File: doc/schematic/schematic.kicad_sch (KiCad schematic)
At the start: 22 parts, among them J1 Power, J10 Screw_Terminal_01x02, J11 UART, J12 UART, J13 Power, J14 Conn_01x02_Pin, J15 FX35, J16 FX35, J17 Load, J2 TFT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

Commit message: Schema V0.1
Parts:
- removed J1: Power, symbol Connector:Conn_01x02_Pin
- removed J2: TFT, symbol Connector:Conn_01x06_Pin
- removed J3: TFT_Power, symbol Connector:Conn_01x02_Socket
- removed J4: TFT, symbol Connector:Conn_01x06_Socket
- removed J5: USB_B_Mini, symbol Connector:USB_B_Mini
- added J1: TFT_Power, Connector_Molex:Molex_KK-254_AE-6410-03A_1x03_P2.54mm_Vertical, symbol Connector:Conn_01x03_Pin
- added J18: USB, Connector_Molex:Molex_KK-254_AE-6410-02A_1x02_P2.54mm_Vertical, symbol Connector:Conn_01x02_Pin
- added J19: Switch, Connector_Molex:Molex_KK-254_AE-6410-02A_1x02_P2.54mm_Vertical, symbol Connector:Conn_01x02_Pin
- added J2: Conn_01x03_Socket, Connector_Molex:Molex_KK-254_AE-6410-03A_1x03_P2.54mm_Vertical, symbol Connector:Conn_01x03_Socket
- added J20, J21: Conn_01x02_Socket, symbol Connector:Conn_01x02_Socket
- added J3: TFT, Connector_Molex:Molex_KK-254_AE-6410-05A_1x05_P2.54mm_Vertical, symbol Connector:Conn_01x05_Pin
- added J4: Conn_01x05_Socket, symbol Connector:Conn_01x05_Socket
- added J5: USB_C_PowerOnly, symbol Connector:USB_C_Receptacle_PowerOnly_6P
- added SW1: SW_DIP_x01, symbol Switch:SW_DIP_x01
- J14: footprint (none) -> Connector_Molex:Molex_KK-254_AE-6410-02A_1x02_P2.54mm_Vertical
- J15: footprint (none) -> Connector_Molex:Molex_KK-254_AE-6410-05A_1x05_P2.54mm_Vertical
- J7: footprint (none) -> Connector_Molex:Molex_KK-254_AE-6410-04A_1x04_P2.54mm_Vertical
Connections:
- net +3V3: now also U1.2 (3V3), J1.1 (Pin_1), J1.2 (Pin_2)
- net +5V: now also J19.2 (Pin_2)
- net GND: now also U1.22 (GND), U1.23 (GND), U1.24 (GND), U1.44 (GND), J1.3 (Pin_3), J18.1 (Pin_1)
- net at U2.7 (LED): now also J2.2 (Pin_2)
- net at U2.11 (RESET): now also J4.1 (Pin_1)
- net at U2.10 (DC/RS): now also J4.2 (Pin_2)
- net at U2.12 (CS): now also J4.3 (Pin_3)
- net at U2.9 (SOI(MOSI)): now also J4.4 (Pin_4)
- net at U2.8 (SCK): now also J4.5 (Pin_5)
- net at U1.12 (GPIO8/ADC1_CH7): now also J3.1 (Pin_1)
- net at U1.15 (GPIO9/ADC1_CH8): now also J3.2 (Pin_2)
- net at U1.16 (GPIO10/ADC1_CH9): now also J3.3 (Pin_3)
- net at U1.17 (GPIO11/ADC2_CH0): now also J3.4 (Pin_4)
- net at U1.18 (GPIO12/ADC2_CH1): now also J3.5 (Pin_5)
- net at U2.13 (GND): now also J2.3 (Pin_3)
- net at U2.14 (VCC): now also J2.1 (Pin_1)
- new net: J21.2 (Pin_2), SW1.1
- new net: J21.1 (Pin_1), SW1.2
- new net: J20.2 (Pin_2), J5.1 (VBUS)
- new net: J20.1 (Pin_1), J5.2 (GND)
- new net: J18.2 (Pin_2), J19.1 (Pin_1)
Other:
- title: (none) -> mGaugeESP
- moved on the sheet: J10, J6, J7, J8, J9, U3, U4

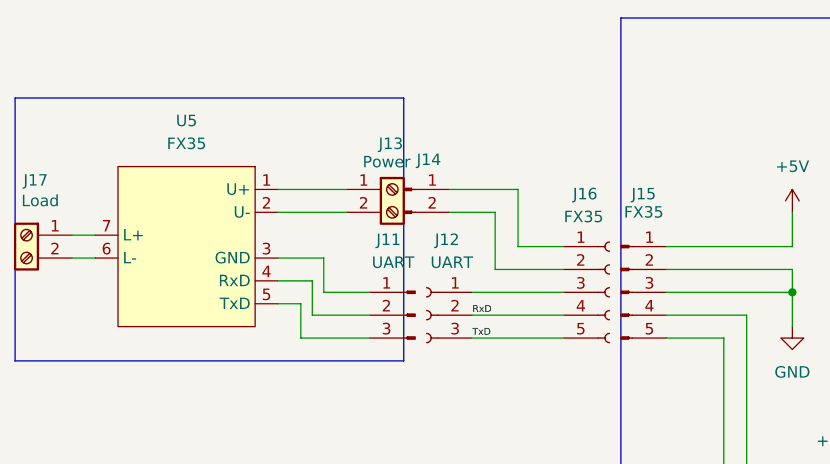
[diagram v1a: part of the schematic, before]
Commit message: Add 2nd INA219 & modify display.
ToDo: implementation of FZ35
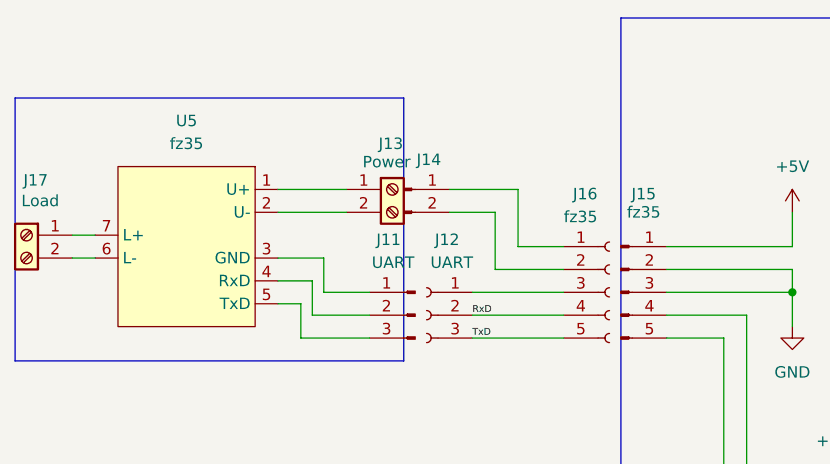
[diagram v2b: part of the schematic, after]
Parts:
- J15, J16: value FX35 -> fz35
- U5: value FX35 -> fz35; symbol MyKiCadLib:xy_FX35 -> MyKiCadLib:xy_fz35
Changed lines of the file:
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@@
 			)
 		)
-		(property "Value" "FX35"
+		(property "Value" "fz35"
 			(at 92.71 39.37 0)
 			(effects
@@
 	)
 	(symbol
-		(lib_id "MyKiCadLib:xy_FX35")
+		(lib_id "MyKiCadLib:xy_fz35")
 		(at 41.91 41.91 0)
 		(unit 1)
@@
 			)
 		)
-		(property "Value" "FX35"
+		(property "Value" "fz35"
 			(at 41.91 31.75 0)
 			(effects
@@
 			)
 		)
-		(property "Value" "FX35"
+		(property "Value" "fz35"
 			(at 83.82 39.878 0)
 			(effects

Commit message: full functionality
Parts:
- added J22: Fan, Connector_Molex:Molex_KK-254_AE-6410-02A_1x02_P2.54mm_Vertical, symbol Connector:Conn_01x02_Pin
- added J23: Conn_01x02_Socket, symbol Connector:Conn_01x02_Socket
- added M1: Fan, symbol Motor:Fan
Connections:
- net +5V: now also J22.1 (Pin_1)
- net GND: now also J22.2 (Pin_2); no longer U1.23 (GND), U1.24 (GND)
- net at J6.1 (Pin_1), U3.5 (VS), U4.5 (VS): now also U3.2 (A0)
- net at U3.3 (SDA), U4.3 (SDA): now also J6.4 (Pin_4); no longer J6.3 (Pin_3)
- net at U3.4 (SCL), U4.4 (SCL): now also J6.3 (Pin_3); no longer J6.4 (Pin_4)
- net at J7.3 (Pin_3): now also U1.40 (GPIO2/ADC1_CH1); no longer U1.33 (GPIO36)
- net at J7.4 (Pin_4): now also U1.41 (GPIO1/ADC1_CH0); no longer U1.32 (GPIO35)
- new net: J23.1 (Pin_1), M1.1 (+)
- new net: J23.2 (Pin_2), M1.2 (-)
- no-connect marks 0 -> 11
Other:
- moved on the sheet: J1, J10, J11, J12, J13, J14, J15, J16, J17, J18, J19, J2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

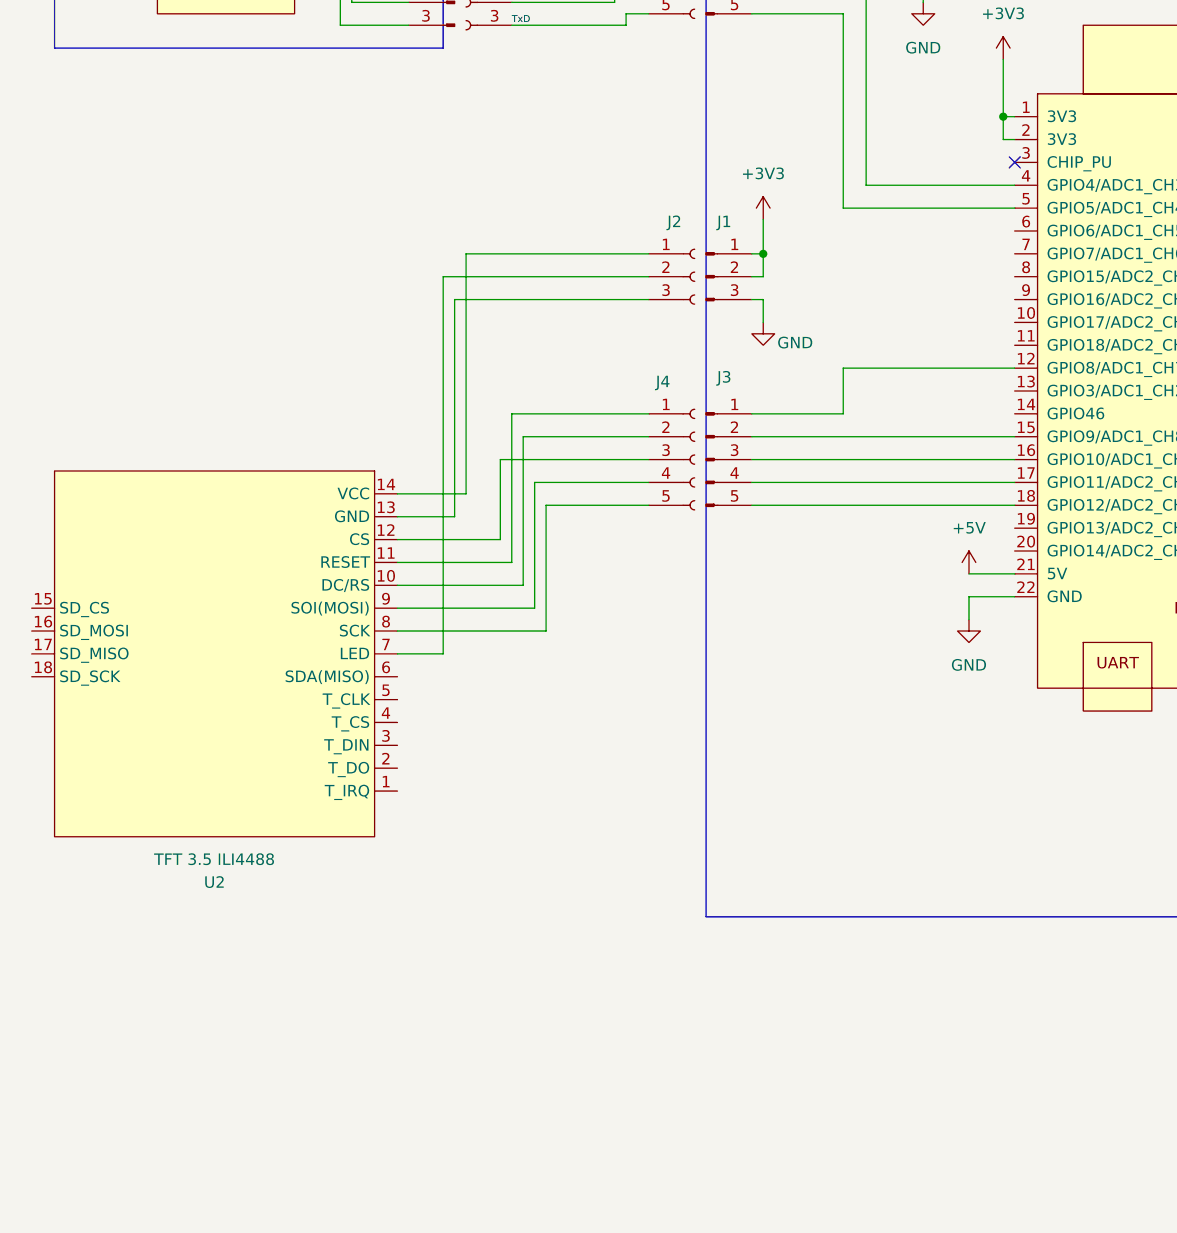
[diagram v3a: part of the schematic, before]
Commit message: code optimization
1.) centralization of data in a global class
2.) make Display as a global class
3.) code optimization
4.) prepare for a setup dialog

this version not able for production
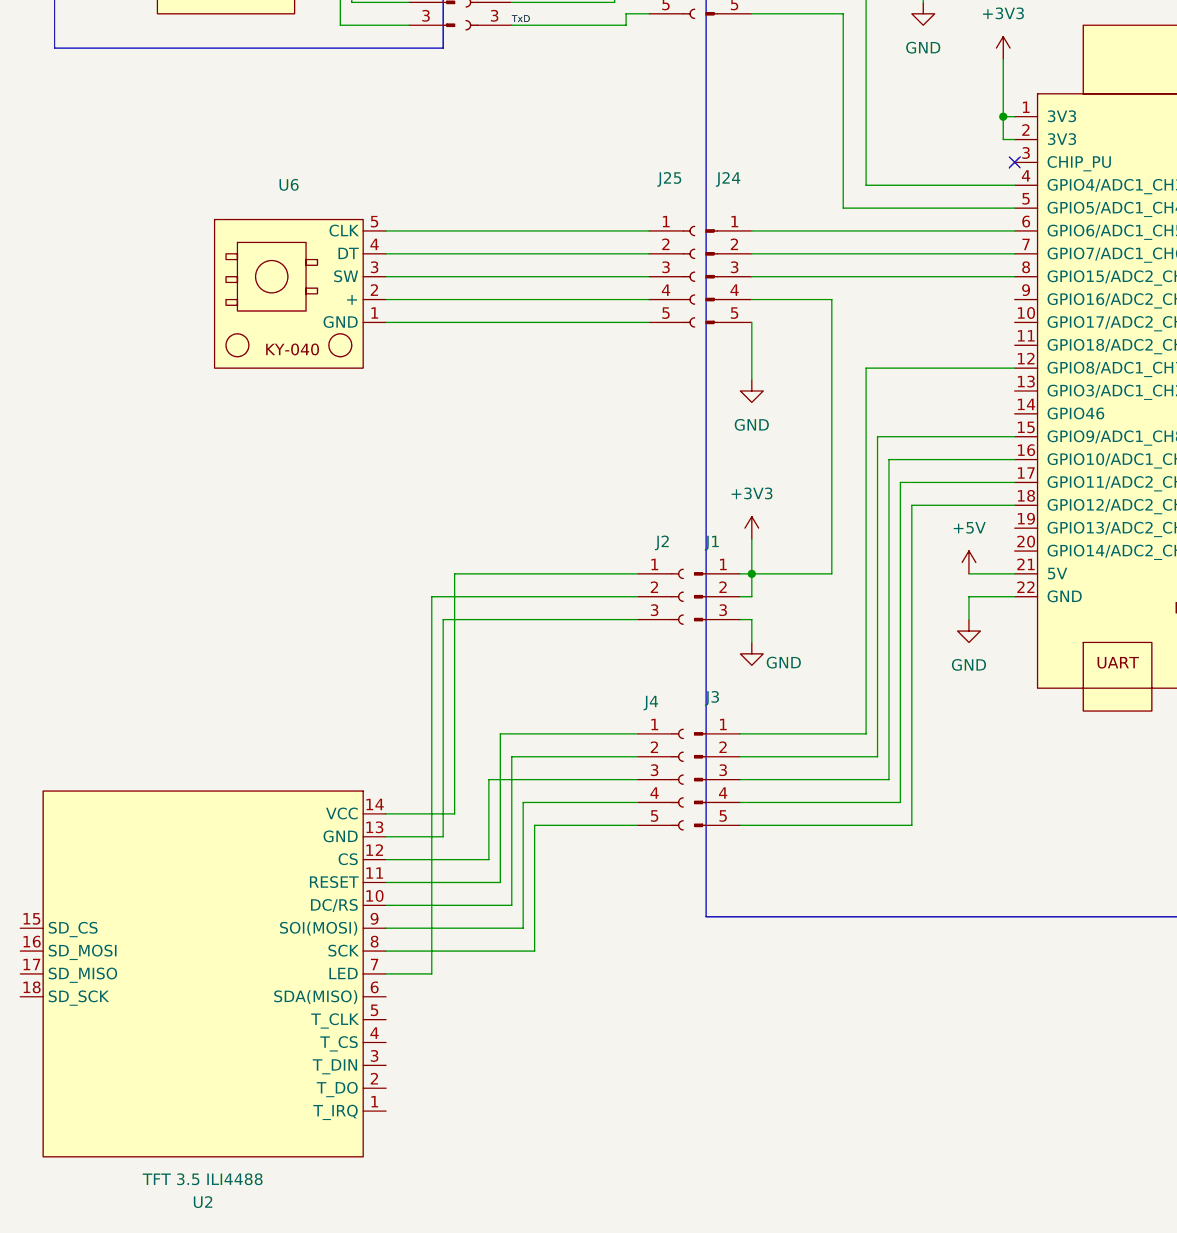
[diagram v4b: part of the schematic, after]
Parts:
- added J24: KY-040, Connector_Molex:Molex_KK-254_AE-6410-05A_1x05_P2.54mm_Vertical, symbol Connector:Conn_01x05_Pin
- added J25: KY-040, symbol Connector:Conn_01x05_Socket
- added U6: ~, symbol MyKiCadLib:KY-040
- J14: footprint Connector_Molex:Molex_KK-254_AE-6410-02A_1x02_P2.54mm_Vertical -> (none)
- J2: footprint Connector_Molex:Molex_KK-254_AE-6410-03A_1x03_P2.54mm_Vertical -> (none)
- U1: footprint PCM_Espressif:ESP32-S3-DevKitC -> Library:ESP32-S3-DevKitC
- U3, U4: footprint Package_SO:SOIC-8_3.9x4.9mm_P1.27mm -> (none)
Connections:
- net +3V3: now also J24.4 (Pin_4)
- net GND: now also J24.5 (Pin_5)
- net at U1.6 (GPIO6/ADC1_CH5): now also J24.1 (Pin_1)
- net at U1.7 (GPIO7/ADC1_CH6): now also J24.2 (Pin_2)
- net at U1.8 (GPIO15/ADC2_CH4/32K_P): now also J24.3 (Pin_3)
- new net: J25.5 (Pin_5), U6.1 (GND)
- new net: J25.4 (Pin_4), U6.2 (+)
- new net: J25.3 (Pin_3), U6.3 (SW)
- new net: J25.2 (Pin_2), U6.4 (DT)
- new net: J25.1 (Pin_1), U6.5 (CLK)
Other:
- moved on the sheet: J1, J2, J3, J4, U2

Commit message: Bug Fix for V1.0.0-pre_alpha
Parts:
- added C1: 0,1µ, Capacitor_THT:C_Axial_L3.8mm_D2.6mm_P7.50mm_Horizontal, symbol Device:C
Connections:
- net +3V3: now also J7.4 (Pin_4); no longer J7.1 (Pin_1)
- net +5V: now also C1.1
- net GND: now also J7.3 (Pin_3), C1.2; no longer J7.2 (Pin_2)
- net at J24.1 (Pin_1): now also U1.8 (GPIO15/ADC2_CH4/32K_P); no longer U1.6 (GPIO6/ADC1_CH5)
- net at J24.3 (Pin_3): now also U1.6 (GPIO6/ADC1_CH5); no longer U1.8 (GPIO15/ADC2_CH4/32K_P)
- net at U3.2 (A0), U3.5 (VS), U4.5 (VS): now also J6.4 (Pin_4); no longer J6.1 (Pin_1)
- net at J10.1 (Pin_1), J10.2 (Pin_2), U3.6 (GND)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: now also J6.3 (Pin_3); no longer J6.2 (Pin_2)
- net at U3.4 (SCL), U4.4 (SCL): now also J6.2 (Pin_2); no longer J6.3 (Pin_3)
- net at U3.3 (SDA), U4.3 (SDA): now also J6.1 (Pin_1); no longer J6.4 (Pin_4)
- net at U1.40 (GPIO2/ADC1_CH1): now also J7.1 (Pin_1); no longer J7.3 (Pin_3)
- net at U1.41 (GPIO1/ADC1_CH0): now also J7.2 (Pin_2); no longer J7.4 (Pin_4)
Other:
- moved on the sheet: J6, J7
